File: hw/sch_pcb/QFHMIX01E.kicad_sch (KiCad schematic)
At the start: 81 parts, among them J1 HEADER_1x08, J2 +9V, M1 HOLE, M2 HOLE, M3 HOLE, M4 HOLE, M5 HOLE, M6 HOLE, M7 HOLE, M8 HOLE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

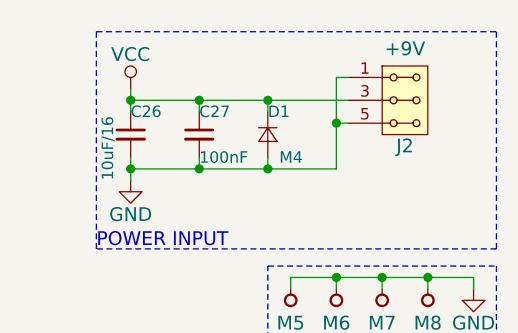
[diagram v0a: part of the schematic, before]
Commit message: Define footprints of new components and update PCB.
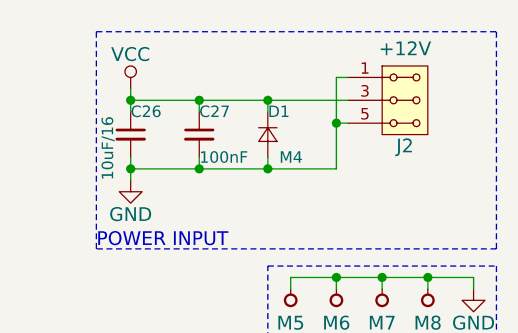
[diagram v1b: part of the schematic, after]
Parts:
- J2: value +9V -> +12V

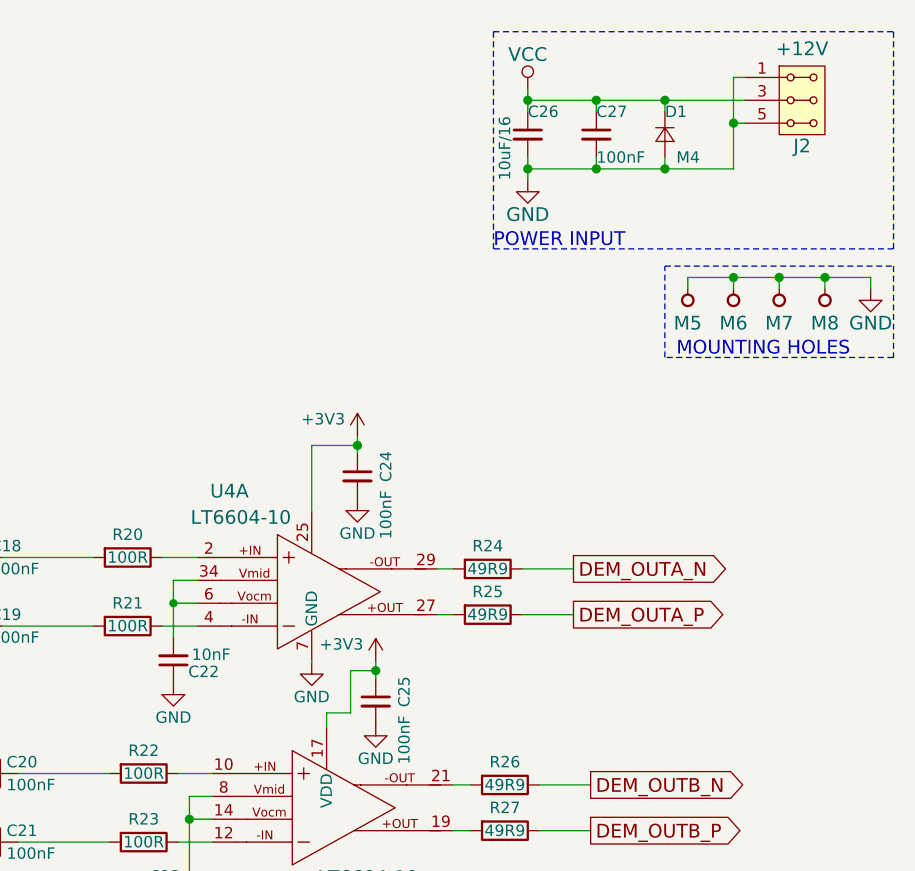
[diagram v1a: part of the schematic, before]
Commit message: Grouping components according to function.
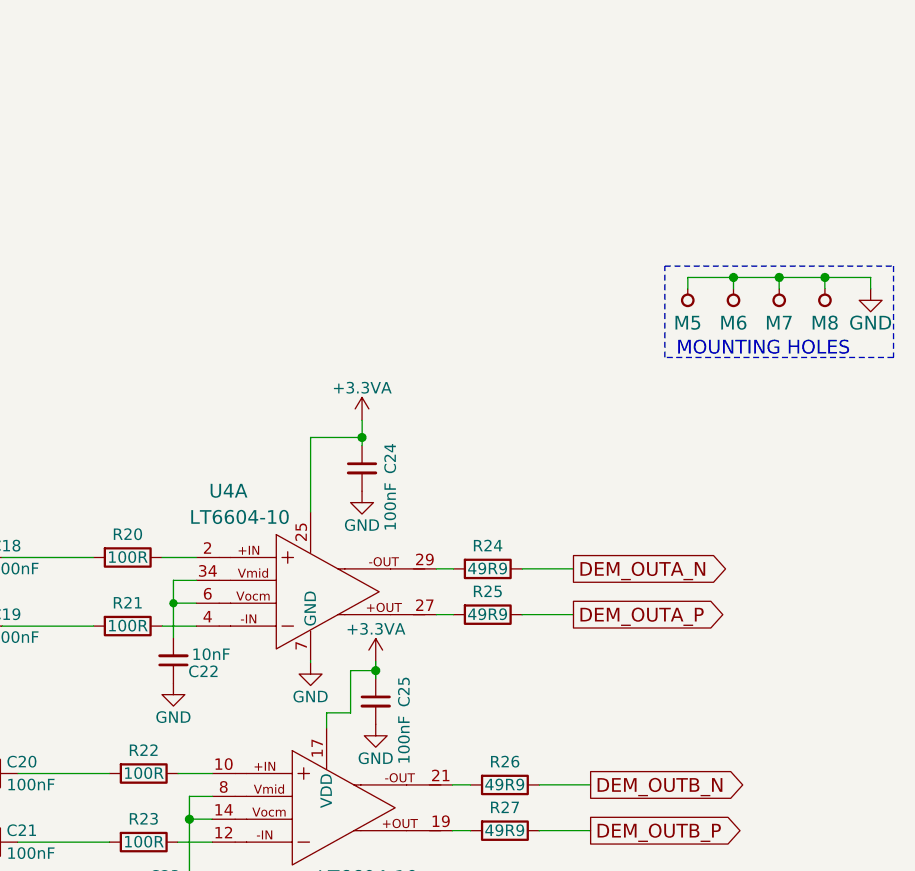
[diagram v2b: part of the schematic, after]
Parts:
- removed C26: 10uF/16, Capacitor_SMD:C_0805_2012Metric, symbol QFHMIX01C-rescue:C_Small-device-QFHMIX01B-rescue
- removed C27: 100nF, Capacitor_SMD:C_0603_1608Metric, symbol QFHMIX01C-rescue:C_Small-device-QFHMIX01B-rescue
- removed D1: M4, Diode_SMD:D_SMA, symbol QFHMIX01C-rescue:D_Small-device-QFHMIX01B-rescue
- removed J2: +12V, Mlab_Pin_Headers:Straight_2x03, symbol QFHMIX01C-rescue:HEADER_2x03_PARALLEL-MLAB_HEADER
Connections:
- net +3V3: no longer C24.1, C25.1, U4.17 (VDD), U4.25
- new net +3.3VA: C24.1, C25.1, U4.17 (VDD), U4.25
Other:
- note removed: "POWER INPUT"
- moved on the sheet: C24

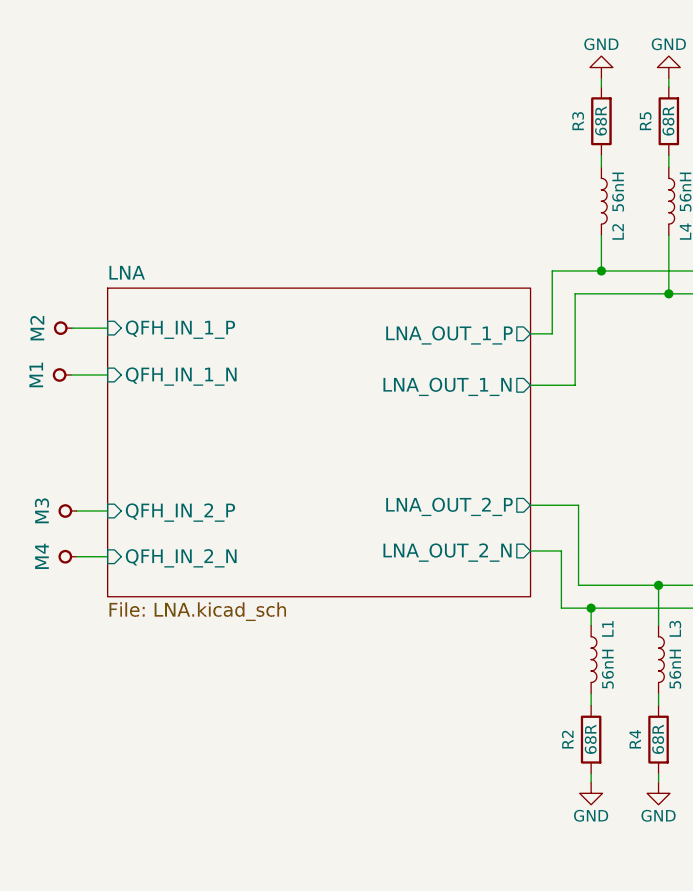
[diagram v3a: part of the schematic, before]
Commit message: Removed duplicite copper pour.
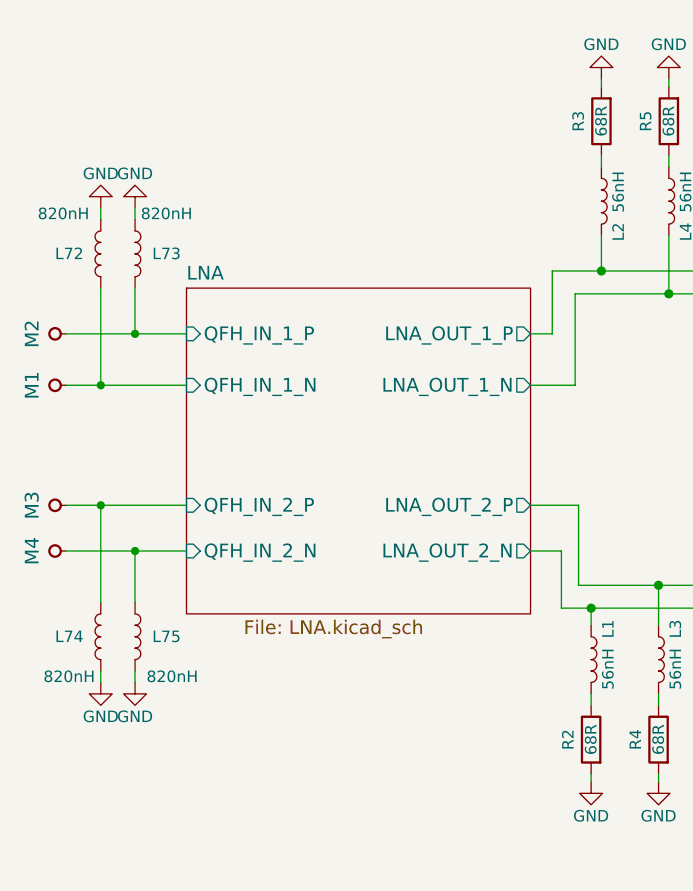
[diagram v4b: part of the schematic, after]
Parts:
- added L72, L73, L74, L75: 820nH, Inductor_SMD:L_0805_2012Metric_Pad1.15x1.40mm_HandSolder, symbol QFHMIX01C-rescue:L-device-QFHMIX01B-rescue
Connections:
- net GND: now also L72.2, L73.2, L74.2, L75.2
- net LNA/QFH_IN_1_N: now also L72.1
- net LNA/QFH_IN_1_P: now also L73.1
- net LNA/QFH_IN_2_N: now also L75.1
- net LNA/QFH_IN_2_P: now also L74.1
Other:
- moved on the sheet: M1, M2, M3, M4
